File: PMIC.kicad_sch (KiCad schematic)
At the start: 0 parts

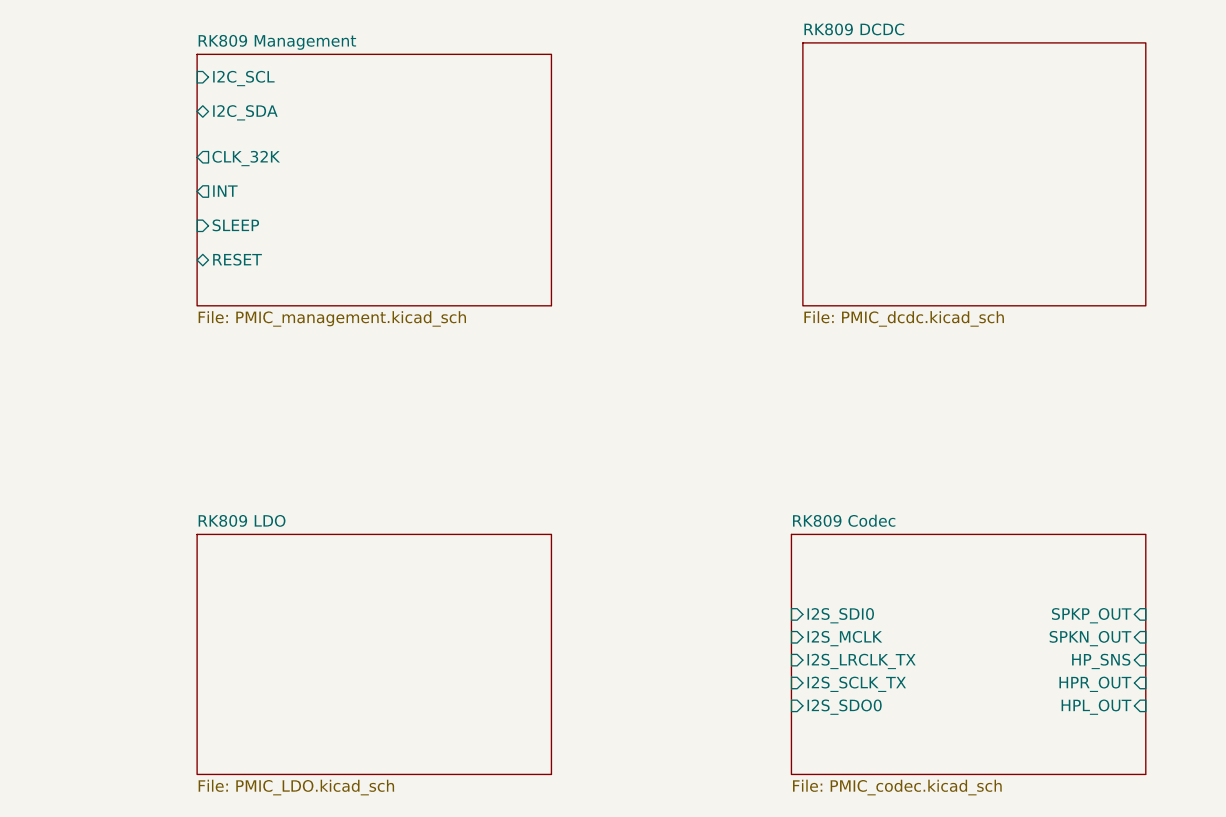
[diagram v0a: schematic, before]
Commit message: fix some ERCs
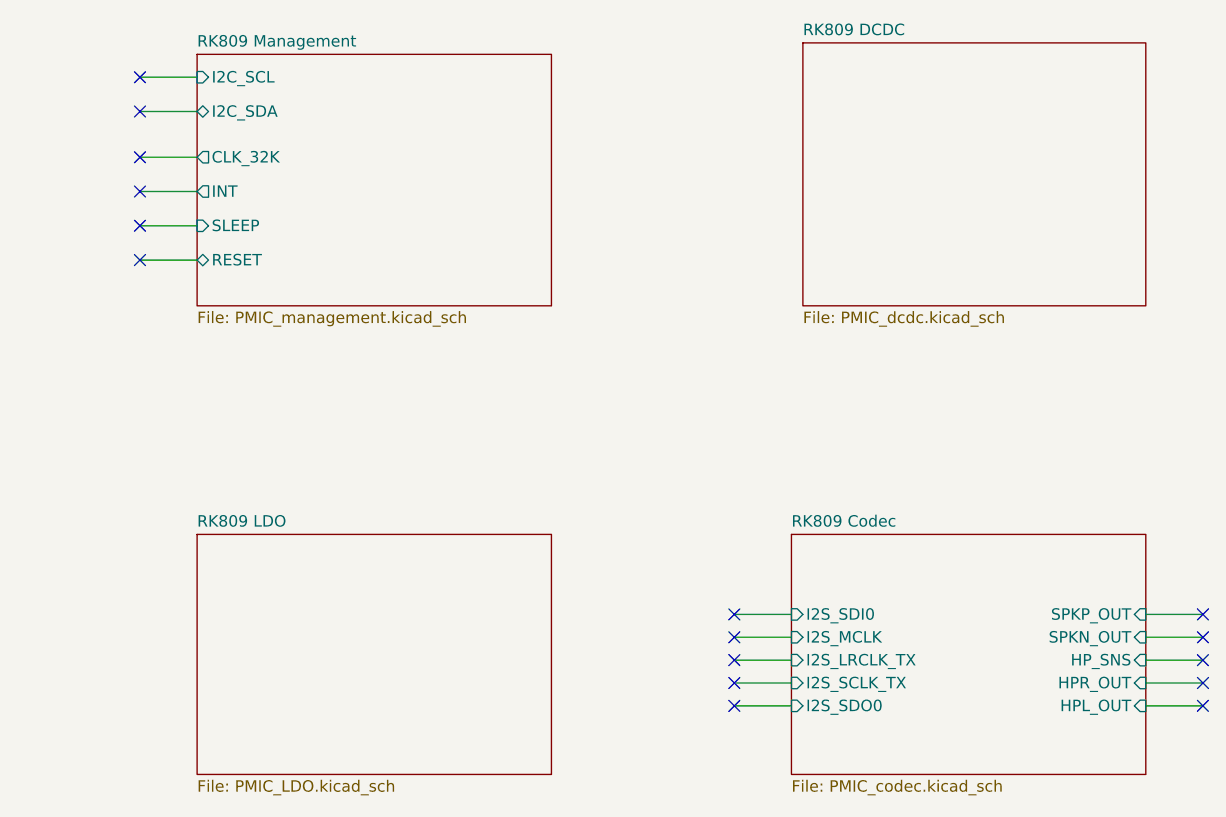
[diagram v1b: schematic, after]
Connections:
- no-connect marks 0 -> 16
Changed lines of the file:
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@@
     (company "Qingdao IotPi Information Technology")
+  )
+  (no_connect (at 160.02 109.22))
+  (no_connect (at 41.91 59.69))
+  (no_connect (at 41.91 55.88))
+  (no_connect (at 107.95 114.3))
+  (no_connect (at 160.02 111.76))
+  (no_connect (at 107.95 111.76))
+  (no_connect (at 160.02 106.68))
+  (no_connect (at 41.91 63.5))
+  (no_connect (at 107.95 116.84))
+  (no_connect (at 41.91 50.8))
+  (no_connect (at 41.91 46.99))
+  (no_connect (at 107.95 106.68))
+  (no_connect (at 41.91 67.31))
+  (no_connect (at 160.02 116.84))
+  (no_connect (at 160.02 114.3))
+  (no_connect (at 107.95 109.22))
+  (wire (pts (xy 160.02 111.76) (xy 153.67 111.76))
+    (stroke (width 0) (type default))
+  )
+  (wire (pts (xy 107.95 114.3) (xy 114.3 114.3))
+    (stroke (width 0) (type default))
+  )
+  (wire (pts (xy 160.02 109.22) (xy 153.67 109.22))
+    (stroke (width 0) (type default))
+  )
+  (wire (pts (xy 107.95 109.22) (xy 114.3 109.22))
+    (stroke (width 0) (type default))
+  )
+  (wire (pts (xy 160.02 114.3) (xy 153.67 114.3))
+    (stroke (width 0) (type default))
+  )
+  (wire (pts (xy 41.91 67.31) (xy 48.26 67.31))
+    (stroke (width 0) (type default))
+  )
+  (wire (pts (xy 41.91 63.5) (xy 48.26 63.5))
+    (stroke (width 0) (type default))
+  )
+  (wire (pts (xy 41.91 46.99) (xy 48.26 46.99))
+    (stroke (width 0) (type default))
+  )
+  (wire (pts (xy 41.91 59.69) (xy 48.26 59.69))
+    (stroke (width 0) (type default))
+  )
+  (wire (pts (xy 160.02 116.84) (xy 153.67 116.84))
+    (stroke (width 0) (type default))
+  )
+  (wire (pts (xy 160.02 106.68) (xy 153.67 106.68))
+    (stroke (width 0) (type default))
+  )
+  (wire (pts (xy 107.95 106.68) (xy 114.3 106.68))
+    (stroke (width 0) (type default))
+  )
+  (wire (pts (xy 107.95 111.76) (xy 114.3 111.76))
+    (stroke (width 0) (type default))
+  )
+  (wire (pts (xy 41.91 50.8) (xy 48.26 50.8))
+    (stroke (width 0) (type default))
+  )
+  (wire (pts (xy 107.95 116.84) (xy 114.3 116.84))
+    (stroke (width 0) (type default))
+  )
+  (wire (pts (xy 41.91 55.88) (xy 48.26 55.88))
+    (stroke (width 0) (type default))
   )
   (sheet (at 115.57 43.18) (size 38.1 29.21) (fields_autoplaced)

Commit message: updated symbols
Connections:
- no-connect marks 16 -> 5
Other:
- sheet RK809 Codec ports: added none; removed I2S_LRCLK_TX, I2S_MCLK, I2S_SCLK_TX, I2S_SDI0, I2S_SDO0
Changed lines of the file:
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@@
   )
   (no_connect (at 160.02 109.22))
-  (no_connect (at 41.91 59.69))
-  (no_connect (at 41.91 55.88))
-  (no_connect (at 107.95 114.3))
   (no_connect (at 160.02 111.76))
-  (no_connect (at 107.95 111.76))
   (no_connect (at 160.02 106.68))
-  (no_connect (at 41.91 63.5))
-  (no_connect (at 107.95 116.84))
-  (no_connect (at 41.91 50.8))
-  (no_connect (at 41.91 46.99))
-  (no_connect (at 107.95 106.68))
-  (no_connect (at 41.91 67.31))
   (no_connect (at 160.02 116.84))
   (no_connect (at 160.02 114.3))
-  (no_connect (at 107.95 109.22))
   (wire (pts (xy 160.02 111.76) (xy 153.67 111.76))
-    (stroke (width 0) (type default))
-  )
-  (wire (pts (xy 107.95 114.3) (xy 114.3 114.3))
     (stroke (width 0) (type default))
   )
@@
     (stroke (width 0) (type default))
   )
-  (wire (pts (xy 107.95 109.22) (xy 114.3 109.22))
-    (stroke (width 0) (type default))
-  )
   (wire (pts (xy 160.02 114.3) (xy 153.67 114.3))
     (stroke (width 0) (type default))
   )
-  (wire (pts (xy 41.91 67.31) (xy 48.26 67.31))
-    (stroke (width 0) (type default))
-  )
-  (wire (pts (xy 41.91 63.5) (xy 48.26 63.5))
-    (stroke (width 0) (type default))
-  )
-  (wire (pts (xy 41.91 46.99) (xy 48.26 46.99))
-    (stroke (width 0) (type default))
-  )
-  (wire (pts (xy 41.91 59.69) (xy 48.26 59.69))
+  (wire (pts (xy 39.37 67.31) (xy 48.26 67.31))
     (stroke (width 0) (type default))
   )
@@
     (stroke (width 0) (type default))
   )
-  (wire (pts (xy 107.95 106.68) (xy 114.3 106.68))
+  (wire (pts (xy 39.37 59.69) (xy 48.26 59.69))
     (stroke (width 0) (type default))
   )
-  (wire (pts (xy 107.95 111.76) (xy 114.3 111.76))
+  (wire (pts (xy 39.37 50.8) (xy 48.26 50.8))
     (stroke (width 0) (type default))
   )
-  (wire (pts (xy 41.91 50.8) (xy 48.26 50.8))
+  (wire (pts (xy 39.37 63.5) (xy 48.26 63.5))
     (stroke (width 0) (type default))
   )
-  (wire (pts (xy 107.95 116.84) (xy 114.3 116.84))
+  (wire (pts (xy 39.37 46.99) (xy 48.26 46.99))
     (stroke (width 0) (type default))
   )
-  (wire (pts (xy 41.91 55.88) (xy 48.26 55.88))
+  (wire (pts (xy 39.37 55.88) (xy 48.26 55.88))
     (stroke (width 0) (type default))
+  )
+  (hierarchical_label "INT" (shape output) (at 39.37 59.69 180) (fields_autoplaced)
+    (effects (font (size 1.27 1.27)) (justify right))
+  )
+  (hierarchical_label "CLK_32K" (shape output) (at 39.37 55.88 180) (fields_autoplaced)
+    (effects (font (size 1.27 1.27)) (justify right))
+  )
+  (hierarchical_label "I2C_SCL" (shape input) (at 39.37 46.99 180) (fields_autoplaced)
+    (effects (font (size 1.27 1.27)) (justify right))
+  )
+  (hierarchical_label "RESET" (shape bidirectional) (at 39.37 67.31 180) (fields_autoplaced)
+    (effects (font (size 1.27 1.27)) (justify right))
+  )
+  (hierarchical_label "I2C_SDA" (shape bidirectional) (at 39.37 50.8 180) (fields_autoplaced)
+    (effects (font (size 1.27 1.27)) (justify right))
+  )
+  (hierarchical_label "SLEEP" (shape input) (at 39.37 63.5 180) (fields_autoplaced)
+    (effects (font (size 1.27 1.27)) (justify right))
   )
   (sheet (at 115.57 43.18) (size 38.1 29.21) (fields_autoplaced)
@@
       (effects (font (size 1.27 1.27)) (justify right))
     )
-    (pin "I2S_SDI0" input (at 114.3 106.68 180)
-      (effects (font (size 1.27 1.27)) (justify left))
-    )
     (pin "SPKP_OUT" input (at 153.67 106.68 0)
       (effects (font (size 1.27 1.27)) (justify right))
     )
-    (pin "I2S_MCLK" input (at 114.3 109.22 180)
-      (effects (font (size 1.27 1.27)) (justify left))
-    )
-    (pin "I2S_LRCLK_TX" input (at 114.3 111.76 180)
-      (effects (font (size 1.27 1.27)) (justify left))
-    )
-    (pin "I2S_SCLK_TX" input (at 114.3 114.3 180)
-      (effects (font (size 1.27 1.27)) (justify left))
-    )
-    (pin "I2S_SDO0" input (at 114.3 116.84 180)
-      (effects (font (size 1.27 1.27)) (justify left))
-    )
     (instances

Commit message: fix errors
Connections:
- no-connect marks 5 -> 10
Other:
- sheet RK809 Codec ports: added I2S_LRCLK_TX, I2S_MCLK, I2S_SCLK_TX, I2S_SDI0, I2S_SDO0; removed none
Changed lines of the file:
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@@
   (no_connect (at 160.02 111.76))
   (no_connect (at 160.02 106.68))
+  (no_connect (at 107.95 106.68))
+  (no_connect (at 107.95 116.84))
   (no_connect (at 160.02 116.84))
+  (no_connect (at 107.95 114.3))
   (no_connect (at 160.02 114.3))
+  (no_connect (at 107.95 109.22))
+  (no_connect (at 107.95 111.76))
   (wire (pts (xy 160.02 111.76) (xy 153.67 111.76))
+    (stroke (width 0) (type default))
+  )
+  (wire (pts (xy 107.95 116.84) (xy 114.3 116.84))
+    (stroke (width 0) (type default))
+  )
+  (wire (pts (xy 107.95 114.3) (xy 114.3 114.3))
     (stroke (width 0) (type default))
   )
@@
     (stroke (width 0) (type default))
   )
+  (wire (pts (xy 107.95 106.68) (xy 114.3 106.68))
+    (stroke (width 0) (type default))
+  )
   (wire (pts (xy 39.37 67.31) (xy 48.26 67.31))
     (stroke (width 0) (type default))
   )
   (wire (pts (xy 160.02 116.84) (xy 153.67 116.84))
+    (stroke (width 0) (type default))
+  )
+  (wire (pts (xy 107.95 111.76) (xy 114.3 111.76))
     (stroke (width 0) (type default))
   )
@@
   )
   (wire (pts (xy 39.37 55.88) (xy 48.26 55.88))
+    (stroke (width 0) (type default))
+  )
+  (wire (pts (xy 107.95 109.22) (xy 114.3 109.22))
     (stroke (width 0) (type default))
   )
@@
       (effects (font (size 1.27 1.27)) (justify right))
     )
+    (pin "I2S_SDI0" input (at 114.3 106.68 180)
+      (effects (font (size 1.27 1.27)) (justify left))
+    )
+    (pin "I2S_SCLK_TX" input (at 114.3 109.22 180)
+      (effects (font (size 1.27 1.27)) (justify left))
+    )
+    (pin "I2S_LRCLK_TX" input (at 114.3 111.76 180)
+      (effects (font (size 1.27 1.27)) (justify left))
+    )
+    (pin "I2S_MCLK" input (at 114.3 114.3 180)
+      (effects (font (size 1.27 1.27)) (justify left))
+    )
+    (pin "I2S_SDO0" input (at 114.3 116.84 180)
+      (effects (font (size 1.27 1.27)) (justify left))
+    )
     (instances

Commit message: fixing warnings
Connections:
- no-connect marks 10 -> 0
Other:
- sheet RK809 Codec ports: added none; removed HPL_OUT, HPR_OUT, HP_SNS, I2S_LRCLK_TX, I2S_MCLK, I2S_SCLK_TX, I2S_SDI0, I2S_SDO0, SPKN_OUT, SPKP_OUT
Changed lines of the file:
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@@
     (company "Qingdao IotPi Information Technology")
   )
-  (no_connect (at 160.02 109.22))
-  (no_connect (at 160.02 111.76))
-  (no_connect (at 160.02 106.68))
-  (no_connect (at 107.95 106.68))
-  (no_connect (at 107.95 116.84))
-  (no_connect (at 160.02 116.84))
-  (no_connect (at 107.95 114.3))
-  (no_connect (at 160.02 114.3))
-  (no_connect (at 107.95 109.22))
-  (no_connect (at 107.95 111.76))
-  (wire (pts (xy 160.02 111.76) (xy 153.67 111.76))
-    (stroke (width 0) (type default))
-  )
-  (wire (pts (xy 107.95 116.84) (xy 114.3 116.84))
-    (stroke (width 0) (type default))
-  )
-  (wire (pts (xy 107.95 114.3) (xy 114.3 114.3))
-    (stroke (width 0) (type default))
-  )
-  (wire (pts (xy 160.02 109.22) (xy 153.67 109.22))
-    (stroke (width 0) (type default))
-  )
-  (wire (pts (xy 160.02 114.3) (xy 153.67 114.3))
-    (stroke (width 0) (type default))
-  )
-  (wire (pts (xy 107.95 106.68) (xy 114.3 106.68))
-    (stroke (width 0) (type default))
-  )
   (wire (pts (xy 39.37 67.31) (xy 48.26 67.31))
-    (stroke (width 0) (type default))
-  )
-  (wire (pts (xy 160.02 116.84) (xy 153.67 116.84))
-    (stroke (width 0) (type default))
-  )
-  (wire (pts (xy 107.95 111.76) (xy 114.3 111.76))
-    (stroke (width 0) (type default))
-  )
-  (wire (pts (xy 160.02 106.68) (xy 153.67 106.68))
     (stroke (width 0) (type default))
   )
@@
   )
   (wire (pts (xy 39.37 55.88) (xy 48.26 55.88))
-    (stroke (width 0) (type default))
-  )
-  (wire (pts (xy 107.95 109.22) (xy 114.3 109.22))
     (stroke (width 0) (type default))
   )
@@
       (effects (font (size 1.27 1.27)) (justify left top))
     )
-    (pin "SPKN_OUT" input (at 153.67 109.22 0)
-      (effects (font (size 1.27 1.27)) (justify right))
-    )
-    (pin "HP_SNS" input (at 153.67 111.76 0)
-      (effects (font (size 1.27 1.27)) (justify right))
-    )
-    (pin "HPR_OUT" input (at 153.67 114.3 0)
-      (effects (font (size 1.27 1.27)) (justify right))
-    )
-    (pin "HPL_OUT" input (at 153.67 116.84 0)
-      (effects (font (size 1.27 1.27)) (justify right))
-    )
-    (pin "SPKP_OUT" input (at 153.67 106.68 0)
-      (effects (font (size 1.27 1.27)) (justify right))
-    )
-    (pin "I2S_SDI0" input (at 114.3 106.68 180)
-      (effects (font (size 1.27 1.27)) (justify left))
-    )
-    (pin "I2S_SCLK_TX" input (at 114.3 109.22 180)
-      (effects (font (size 1.27 1.27)) (justify left))
-    )
-    (pin "I2S_LRCLK_TX" input (at 114.3 111.76 180)
-      (effects (font (size 1.27 1.27)) (justify left))
-    )
-    (pin "I2S_MCLK" input (at 114.3 114.3 180)
-      (effects (font (size 1.27 1.27)) (justify left))
-    )
-    (pin "I2S_SDO0" input (at 114.3 116.84 180)
-      (effects (font (size 1.27 1.27)) (justify left))
-    )
     (instances

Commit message: added README and license
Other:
- company: Qingdao IotPi Information Technology -> Yang Hongbo
- title: Leaf RV1126 PMIC -> Leaf RV1126
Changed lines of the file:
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@@
   (paper "A4")
   (title_block
-    (title "Leaf RV1126 PMIC")
-    (date "2023-02-25")
+    (title "Leaf RV1126")
+    (date "2023-06-07")
     (rev "1")
-    (company "Qingdao IotPi Information Technology")
+    (company "Yang Hongbo")
+    (comment 1 "License: CC BY-SA")
   )
   (wire (pts (xy 39.37 67.31) (xy 48.26 67.31))
